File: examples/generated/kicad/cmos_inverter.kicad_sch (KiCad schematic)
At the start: 4 parts

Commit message: Attempt to create legible symbols.
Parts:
- MN1: symbol examples:MNMOS -> MNMOS
- MP1: symbol examples:MPMOS -> MPMOS
- VDD, VIN: symbol examples:VSOURCE -> VSOURCE
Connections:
- net GND: now also MN1.1 (D), MN1.2 (G), MN1.3 (S), MP1.1 (D), MP1.2 (G), MP1.3 (S), VDD.1 (E1), VDD.2 (E2), VIN.1 (E1), VIN.2 (E2)
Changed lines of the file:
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@@
     (comment 1 "Generated by mixedsig2cad")
   )
-  (symbol (lib_id "examples:VSOURCE") (at 50.00 55.00 0) (unit 1)
+  (symbol (lib_id "VSOURCE") (at 50.00 55.00 0) (unit 1)
     (in_bom yes) (on_board yes)
     (property "Reference" "VDD" (at 50.0 51.19 0)
@@
     )
   )
-  (symbol (lib_id "examples:VSOURCE") (at 50.00 90.00 0) (unit 1)
+  (symbol (lib_id "VSOURCE") (at 50.00 90.00 0) (unit 1)
     (in_bom yes) (on_board yes)
     (property "Reference" "VIN" (at 50.0 86.19 0)
@@
     )
   )
-  (symbol (lib_id "examples:MPMOS") (at 150.00 85.00 0) (unit 1)
+  (symbol (lib_id "MPMOS") (at 150.00 85.00 0) (unit 1)
     (in_bom yes) (on_board yes)
     (property "Reference" "MP1" (at 150.0 81.19 0)
@@
     )
   )
-  (symbol (lib_id "examples:MNMOS") (at 150.00 130.00 0) (unit 1)
+  (symbol (lib_id "MNMOS") (at 150.00 130.00 0) (unit 1)
     (in_bom yes) (on_board yes)
     (property "Reference" "MN1" (at 150.0 126.19 0)
@@
     )
   )
-  (symbol (lib_id "examples:GND") (at 38.00 41.38 0) (unit 1)
+  (symbol (lib_id "GND") (at 38.00 41.38 0) (unit 1)
     (in_bom yes) (on_board yes)
     (property "Reference" "#PWR0001" (at 38.0 37.57 0)
@@
     )
   )
-  (symbol (lib_id "examples:VCC") (at 38.00 56.62 0) (unit 1)
+  (symbol (lib_id "VCC") (at 38.00 56.62 0) (unit 1)
     (in_bom yes) (on_board yes)
     (property "Reference" "#PWR0002" (at 38.0 52.809999999999995 0)

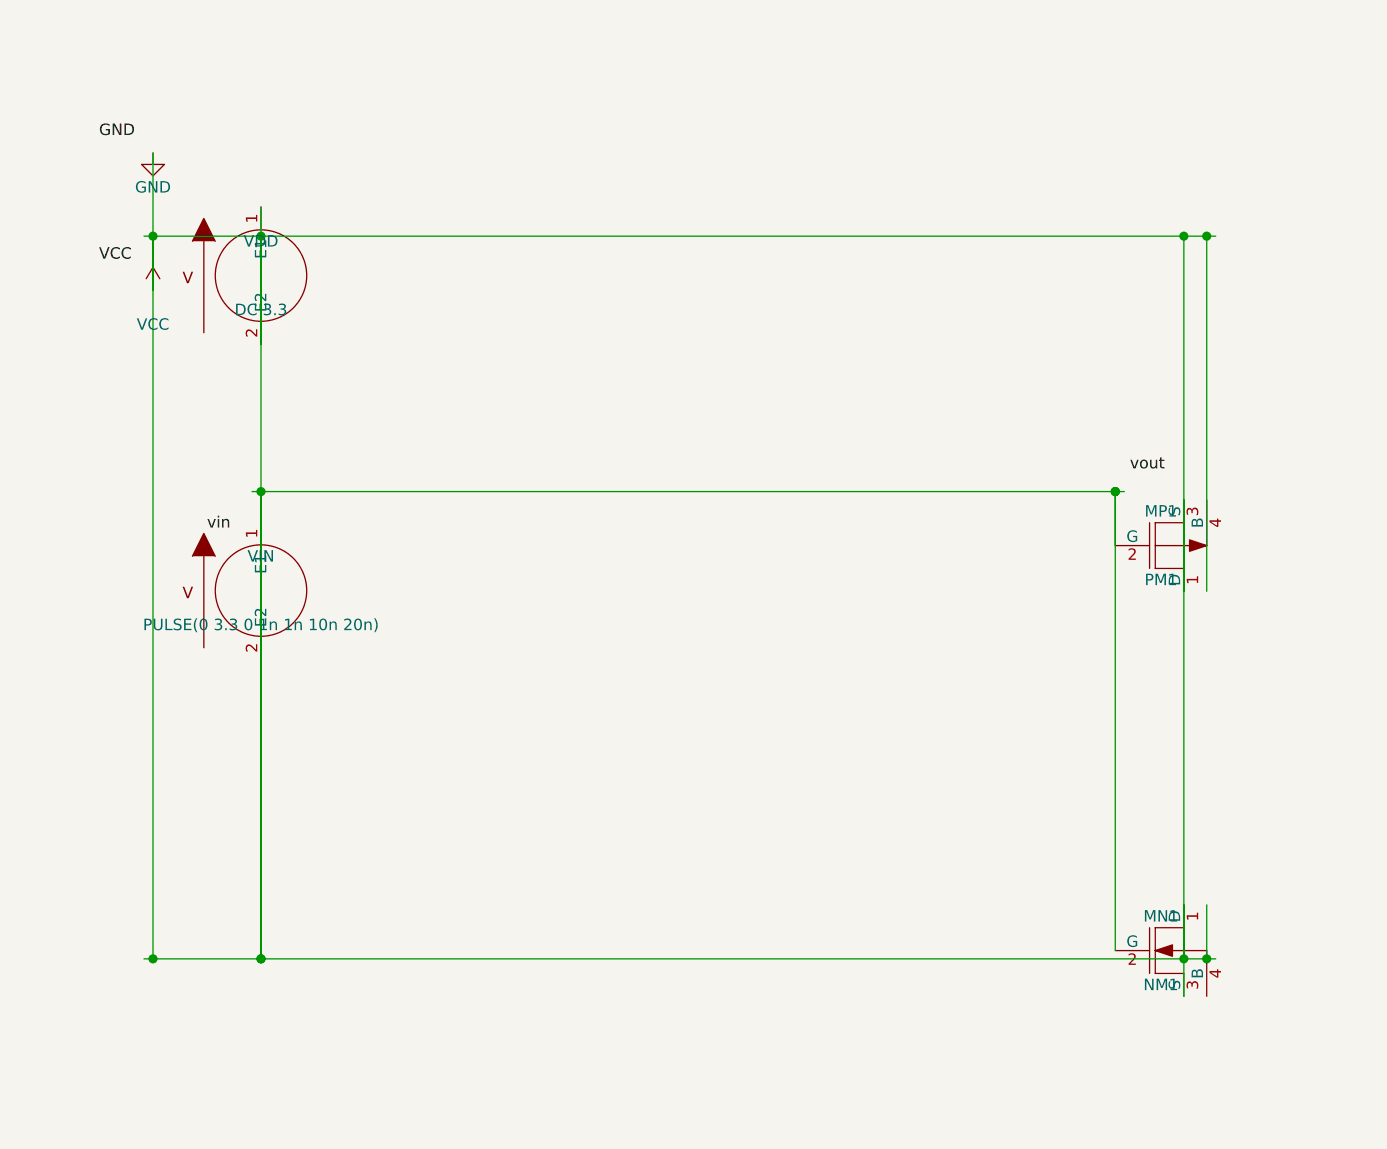
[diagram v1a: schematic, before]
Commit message: Attempt full seperation of circuit concerns into layers.
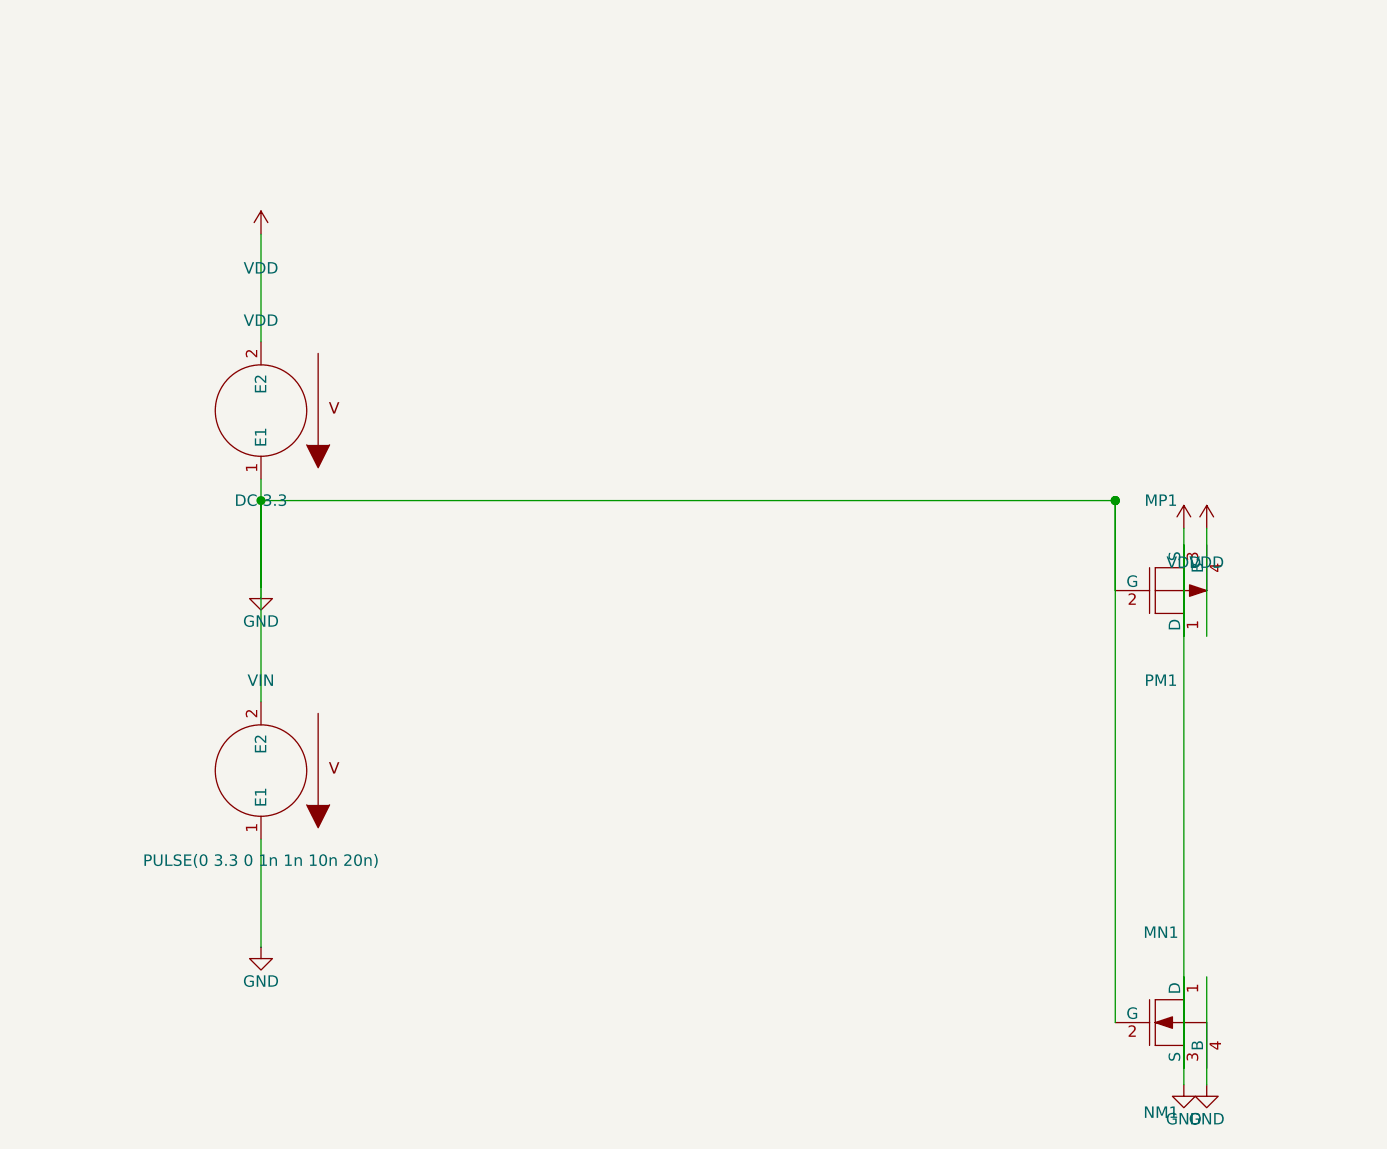
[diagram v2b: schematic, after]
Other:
- moved on the sheet: MN1, MP1, VDD, VIN

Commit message: Add checks for connectivity.
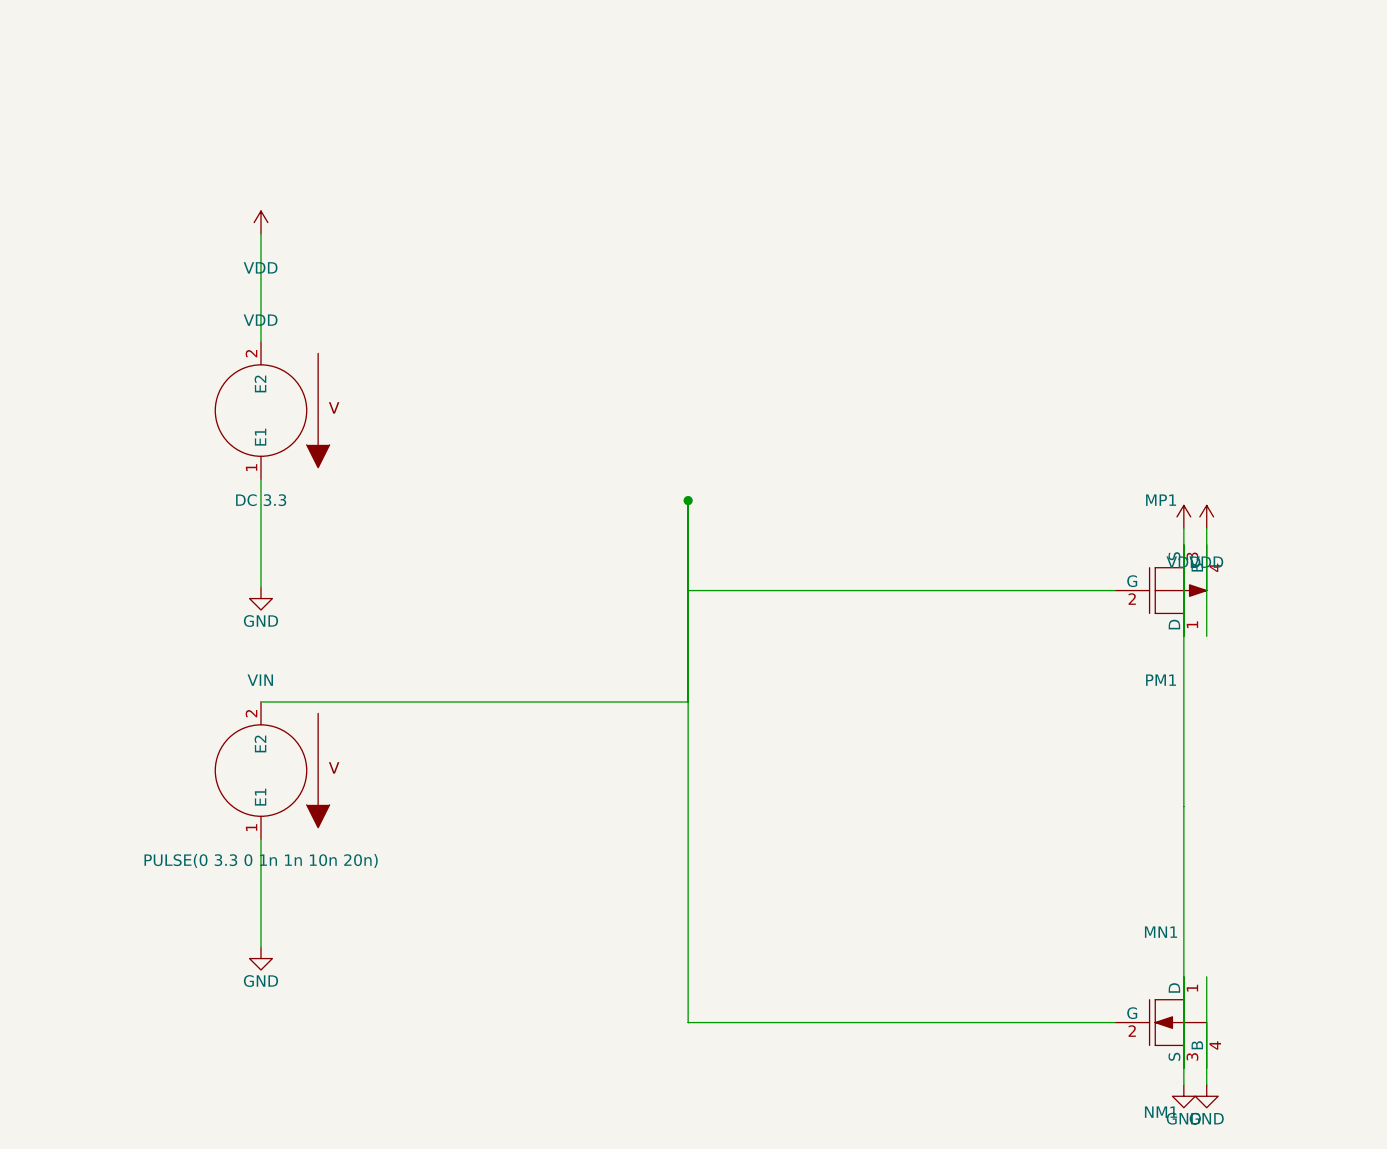
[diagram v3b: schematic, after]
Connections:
- net GND: no longer MN1.2 (G), MP1.2 (G), VIN.2 (E2)
- new net: MN1.2 (G), MP1.2 (G), VIN.2 (E2)
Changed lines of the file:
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@@
     (stroke (width 0) (type solid) (color 0 0 0 0))
   )
-  (wire (pts (xy 50.00 80.00) (xy 144.92 80.00))
+  (wire (pts (xy 50.00 102.38) (xy 97.46 102.38))
     (stroke (width 0) (type solid) (color 0 0 0 0))
   )
-  (wire (pts (xy 50.00 102.38) (xy 50.00 80.00))
+  (wire (pts (xy 97.46 102.38) (xy 97.46 80.00))
     (stroke (width 0) (type solid) (color 0 0 0 0))
   )
-  (wire (pts (xy 144.92 90.00) (xy 144.92 80.00))
+  (wire (pts (xy 144.92 90.00) (xy 97.46 90.00))
     (stroke (width 0) (type solid) (color 0 0 0 0))
   )
-  (wire (pts (xy 144.92 138.00) (xy 144.92 80.00))
+  (wire (pts (xy 97.46 90.00) (xy 97.46 80.00))
     (stroke (width 0) (type solid) (color 0 0 0 0))
   )
-  (wire (pts (xy 152.54 84.92) (xy 152.54 143.08))
+  (wire (pts (xy 144.92 138.00) (xy 97.46 138.00))
     (stroke (width 0) (type solid) (color 0 0 0 0))
   )
-  (junction (at 50.00 80.00) (diameter 1.016) (color 0 0 0 0))
-  (junction (at 144.92 80.00) (diameter 1.016) (color 0 0 0 0))
-  (junction (at 144.92 80.00) (diameter 1.016) (color 0 0 0 0))
+  (wire (pts (xy 97.46 138.00) (xy 97.46 80.00))
+    (stroke (width 0) (type solid) (color 0 0 0 0))
+  )
+  (wire (pts (xy 152.54 84.92) (xy 152.54 114.00))
+    (stroke (width 0) (type solid) (color 0 0 0 0))
+  )
+  (wire (pts (xy 152.54 143.08) (xy 152.54 114.00))
+    (stroke (width 0) (type solid) (color 0 0 0 0))
+  )
+  (junction (at 97.46 80.00) (diameter 1.016) (color 0 0 0 0))
   (sheet_instances
     (path "/" (page "1"))

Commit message: Attempt to correct strange wiring.
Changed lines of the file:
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@@
     )
   )
-  (symbol (lib_id "VCC") (at 152.54 83.08 0) (unit 1)
+  (symbol (lib_id "VCC") (at 140.54 89.08 0) (unit 1)
     (in_bom yes) (on_board yes)
-    (property "Reference" "#PWR0004" (at 152.54 79.27 0)
+    (property "Reference" "#PWR0004" (at 140.54 85.27 0)
       (effects (font (size 1.27 1.27)) hide)
     )
-    (property "Value" "VDD" (at 152.54 86.89 0)
+    (property "Value" "VDD" (at 140.54 92.89 0)
       (effects (font (size 1.27 1.27)))
     )
@@
     )
   )
-  (symbol (lib_id "VCC") (at 155.08 83.08 0) (unit 1)
+  (symbol (lib_id "VCC") (at 167.08 89.08 0) (unit 1)
     (in_bom yes) (on_board yes)
-    (property "Reference" "#PWR0005" (at 155.08 79.27 0)
+    (property "Reference" "#PWR0005" (at 167.08 85.27 0)
       (effects (font (size 1.27 1.27)) hide)
     )
-    (property "Value" "VDD" (at 155.08 86.89 0)
+    (property "Value" "VDD" (at 167.08 92.89 0)
       (effects (font (size 1.27 1.27)))
     )
@@
     )
   )
-  (symbol (lib_id "GND") (at 152.54 144.92 0) (unit 1)
+  (symbol (lib_id "GND") (at 140.54 138.92 0) (unit 1)
     (in_bom yes) (on_board yes)
-    (property "Reference" "#PWR0006" (at 152.54 141.10999999999999 0)
+    (property "Reference" "#PWR0006" (at 140.54 135.10999999999999 0)
       (effects (font (size 1.27 1.27)) hide)
     )
-    (property "Value" "GND" (at 152.54 148.73 0)
+    (property "Value" "GND" (at 140.54 142.73 0)
       (effects (font (size 1.27 1.27)))
     )
@@
     )
   )
-  (symbol (lib_id "GND") (at 155.08 144.92 0) (unit 1)
+  (symbol (lib_id "GND") (at 167.08 138.92 0) (unit 1)
     (in_bom yes) (on_board yes)
-    (property "Reference" "#PWR0007" (at 155.08 141.10999999999999 0)
+    (property "Reference" "#PWR0007" (at 167.08 135.10999999999999 0)
       (effects (font (size 1.27 1.27)) hide)
     )
-    (property "Value" "GND" (at 155.08 148.73 0)
+    (property "Value" "GND" (at 167.08 142.73 0)
       (effects (font (size 1.27 1.27)))
     )
@@
     (stroke (width 0) (type solid) (color 0 0 0 0))
   )
-  (wire (pts (xy 152.54 95.08) (xy 152.54 83.08))
+  (wire (pts (xy 152.54 95.08) (xy 152.54 89.08))
     (stroke (width 0) (type solid) (color 0 0 0 0))
   )
-  (wire (pts (xy 155.08 95.08) (xy 155.08 83.08))
+  (wire (pts (xy 152.54 89.08) (xy 140.54 89.08))
     (stroke (width 0) (type solid) (color 0 0 0 0))
   )
-  (wire (pts (xy 152.54 132.92) (xy 152.54 144.92))
+  (wire (pts (xy 155.08 95.08) (xy 159.50 95.08))
     (stroke (width 0) (type solid) (color 0 0 0 0))
   )
-  (wire (pts (xy 155.08 132.92) (xy 155.08 144.92))
+  (wire (pts (xy 159.50 95.08) (xy 159.50 89.08))
     (stroke (width 0) (type solid) (color 0 0 0 0))
   )
-  (wire (pts (xy 50.00 102.38) (xy 97.46 102.38))
+  (wire (pts (xy 159.50 89.08) (xy 167.08 89.08))
     (stroke (width 0) (type solid) (color 0 0 0 0))
   )
-  (wire (pts (xy 97.46 102.38) (xy 97.46 80.00))
+  (wire (pts (xy 152.54 132.92) (xy 152.54 138.92))
     (stroke (width 0) (type solid) (color 0 0 0 0))
   )
-  (wire (pts (xy 144.92 90.00) (xy 97.46 90.00))
+  (wire (pts (xy 152.54 138.92) (xy 140.54 138.92))
     (stroke (width 0) (type solid) (color 0 0 0 0))
   )
-  (wire (pts (xy 97.46 90.00) (xy 97.46 80.00))
+  (wire (pts (xy 155.08 132.92) (xy 159.50 132.92))
     (stroke (width 0) (type solid) (color 0 0 0 0))
   )
-  (wire (pts (xy 144.92 138.00) (xy 97.46 138.00))
+  (wire (pts (xy 159.50 132.92) (xy 159.50 138.92))
     (stroke (width 0) (type solid) (color 0 0 0 0))
   )
-  (wire (pts (xy 97.46 138.00) (xy 97.46 80.00))
+  (wire (pts (xy 159.50 138.92) (xy 167.08 138.92))
     (stroke (width 0) (type solid) (color 0 0 0 0))
   )
-  (wire (pts (xy 152.54 84.92) (xy 152.54 114.00))
+  (wire (pts (xy 50.00 102.38) (xy 50.00 114.00))
     (stroke (width 0) (type solid) (color 0 0 0 0))
   )
-  (wire (pts (xy 152.54 143.08) (xy 152.54 114.00))
+  (wire (pts (xy 50.00 114.00) (xy 101.25 114.00))
     (stroke (width 0) (type solid) (color 0 0 0 0))
   )
-  (junction (at 97.46 80.00) (diameter 1.016) (color 0 0 0 0))
+  (wire (pts (xy 144.92 90.00) (xy 143.00 90.00))
+    (stroke (width 0) (type solid) (color 0 0 0 0))
+  )
+  (wire (pts (xy 143.00 90.00) (xy 143.00 114.00))
+    (stroke (width 0) (type solid) (color 0 0 0 0))
+  )
+  (wire (pts (xy 143.00 114.00) (xy 101.25 114.00))
+    (stroke (width 0) (type solid) (color 0 0 0 0))
+  )
+  (wire (pts (xy 144.92 138.00) (xy 143.00 138.00))
+    (stroke (width 0) (type solid) (color 0 0 0 0))
+  )
+  (wire (pts (xy 143.00 138.00) (xy 143.00 114.00))
+    (stroke (width 0) (type solid) (color 0 0 0 0))
+  )
+  (wire (pts (xy 143.00 114.00) (xy 101.25 114.00))
+    (stroke (width 0) (type solid) (color 0 0 0 0))
+  )
+  (wire (pts (xy 152.54 84.92) (xy 152.54 143.08))
+    (stroke (width 0) (type solid) (color 0 0 0 0))
+  )
+  (junction (at 101.25 114.00) (diameter 1.016) (color 0 0 0 0))
   (sheet_instances
     (path "/" (page "1"))
